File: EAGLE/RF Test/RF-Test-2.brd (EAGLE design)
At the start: 20.3 x 35.6 mm, 9 parts, among them X1 SMA-142-0701-881/886, X2 IPEX-20279-001E

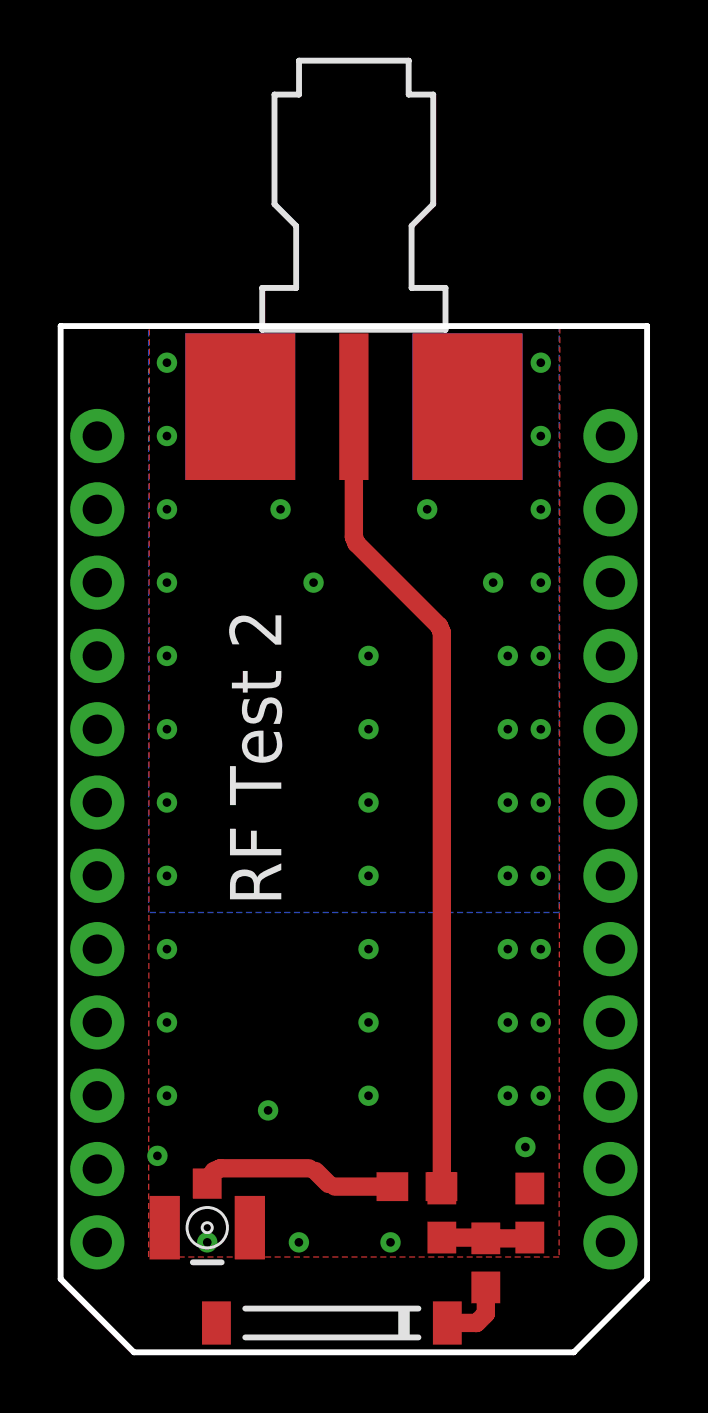
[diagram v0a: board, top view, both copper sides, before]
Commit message: RF Test board updated to match. A0 silk screen moved on core.
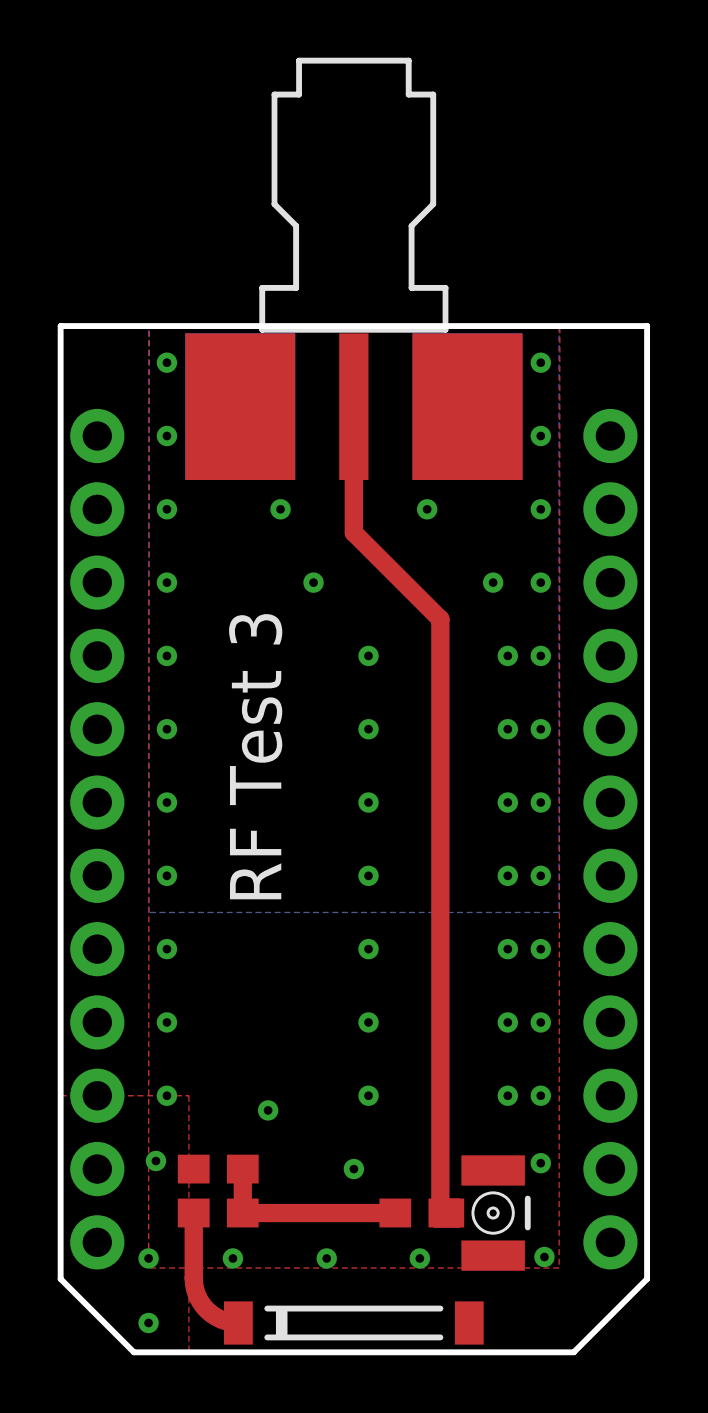
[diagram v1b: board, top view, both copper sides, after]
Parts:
- removed C12, C16: 10pF, rcl:C0603
- added C5: 10pF, rcl:C0603
- moved L1 10.9 mm to (5.46, 3.81), turned to 180 degrees
- moved X2 9.92 mm to (15.0, 2.29), turned to 90 degrees
- moved C4 9.43 mm to (5.46, 2.29), turned to 0 degrees
- moved ANT1 0.76 mm to (10.2, -1.52), turned to 180 degrees
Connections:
- removed net N$2: C16.2, X2.1
- net N$4: now also C5.2, X2.1; no longer C12.2, C16.1
- net N$5: now also C5.1; no longer C12.1
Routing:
- net N$2: track 6.96 -> 0.00 mm
- net N$5: track 3.07 -> 6.81 mm
- net N$3: track 2.38 -> 4.45 mm
- net N$4: track 28.4 -> 29.2 mm
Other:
- board text added: "RF Test 3"
- board text removed: "RF Test 2"
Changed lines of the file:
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@@
 <setting verticaltext="up"/>
 </settings>
-<grid distance="0.05" unitdist="inch" unit="inch" style="lines" multiple="1" display="yes" altdistance="0.005" altunitdist="inch" altunit="inch"/>
+<grid distance="2" unitdist="mil" unit="mil" style="lines" multiple="1" display="yes" altdistance="0.005" altunitdist="inch" altunit="inch"/>
 <layers>
 <layer number="1" name="Top" color="4" fill="1" visible="yes" active="yes"/>
-<layer number="2" name="$GND" color="13" fill="1" visible="no" active="yes"/>
+<layer number="2" name="$GND" color="13" fill="1" visible="yes" active="yes"/>
 <layer number="3" name="Route3" color="4" fill="3" visible="no" active="no"/>
 <layer number="4" name="Route4" color="1" fill="4" visible="no" active="no"/>
@@
 <wire x1="17.78" y1="0.508" x2="17.78" y2="29.21" width="0.2032" layer="51"/>
 <wire x1="2.54" y1="0.508" x2="2.54" y2="29.21" width="0.2032" layer="51"/>
-<text x="5.8674" y="23.2156" size="1.778" layer="21" rot="R270">RF Test 2</text>
+<text x="5.8674" y="23.2156" size="1.778" layer="21" rot="R270">RF Test 3</text>
 </plain>
 <attributes>
@@
 <class number="1" name="vcc" width="0" drill="0">
 </class>
-<class number="2" name="RF" width="0.5842" drill="0">
-<clearance class="2" value="0.762"/>
+<class number="2" name="RF" width="0.635" drill="0">
+<clearance class="2" value="0.635"/>
 </class>
 <class number="3" name="RF2" width="0.5842" drill="0">
@@
 <element name="JP1" library="SparkFun" package="1X12" value="" x="1.27" y="29.21" locked="yes" rot="MR270"/>
 <element name="JP2" library="SparkFun" package="1X12" value="" x="19.05" y="29.21" locked="yes" rot="MR270"/>
-<element name="L1" library="SparkFun-Passives" package="0603" value="2.2nH" x="16.256" y="2.286" smashed="yes" rot="R90">
-<attribute name="VALUE" x="16.51" y="-1.778" size="0.6096" layer="27" font="vector" rot="R90"/>
+<element name="L1" library="SparkFun-Passives" package="0603" value="2.2nH" x="5.461" y="3.81" smashed="yes" rot="R180">
+<attribute name="VALUE" x="9.525" y="4.064" size="0.6096" layer="27" font="vector" rot="R180"/>
 </element>
-<element name="C4" library="rcl" package="C0603" value="2.2pF" x="14.732" y="0.5588" smashed="yes" rot="R90">
-<attribute name="VALUE" x="15.494" y="0.3048" size="0.6096" layer="27"/>
+<element name="C4" library="rcl" package="C0603" value="2.2pF" x="5.461" y="2.286" smashed="yes">
+<attribute name="VALUE" x="5.207" y="1.524" size="0.6096" layer="27" rot="R270"/>
 </element>
-<element name="X2" library="Spark" package="IPEX-20279-001E" value="IPEX-20279-001E" x="5.08" y="1.778"/>
-<element name="C16" library="rcl" package="C0603" value="10pF" x="12.3444" y="3.2004" smashed="yes" rot="R180">
-<attribute name="VALUE" x="12.9794" y="5.1054" size="1.27" layer="27" rot="R180"/>
+<element name="X2" library="Spark" package="IPEX-20279-001E" value="IPEX-20279-001E" x="14.986" y="2.286" rot="R90"/>
+<element name="ANT1" library="Spark" package="AT8010" value="AT8010" x="10.16" y="-1.524" smashed="yes" rot="R180">
+<attribute name="VALUE" x="14.16" y="-0.424" size="0.4064" layer="27" rot="R180"/>
 </element>
-<element name="ANT1" library="Spark" package="AT8010" value="AT8010" x="9.398" y="-1.524" smashed="yes">
-<attribute name="VALUE" x="5.398" y="-2.624" size="0.4064" layer="27"/>
-</element>
-<element name="C12" library="rcl" package="C0603" value="10pF" x="13.208" y="2.286" smashed="yes" rot="R90">
-<attribute name="VALUE" x="15.113" y="1.651" size="1.27" layer="27" rot="R90"/>
+<element name="C5" library="rcl" package="C0603" value="10pF" x="12.446" y="2.286" smashed="yes">
+<attribute name="VALUE" x="11.811" y="0.381" size="1.27" layer="27"/>
 </element>
 <element name="X1" library="andyw-oct-2011" package="ANDYW-GENERIC-END-LAUNCH" value="SMA-142-0701-881/886" x="10.16" y="32.7914" smashed="yes" rot="R270">
@@
 <vertex x="0" y="33.02"/>
 <vertex x="20.32" y="33.02"/>
-<vertex x="20.32" y="0.762"/>
-<vertex x="0" y="0.762"/>
+<vertex x="20.32" y="0.381"/>
+<vertex x="0" y="0.381"/>
 </polygon>
-<via x="3.3528" y="4.2672" extent="1-16" drill="0.3"/>
+<via x="3.302" y="4.0894" extent="1-16" drill="0.3"/>
 <contactref element="X2" pad="2@1"/>
 <contactref element="X2" pad="2@2"/>
-<via x="5.08" y="1.27" extent="1-16" drill="0.3"/>
-<via x="8.255" y="1.27" extent="1-16" drill="0.3"/>
-<via x="11.43" y="1.27" extent="1-16" drill="0.3"/>
+<via x="3.048" y="-1.524" extent="1-16" drill="0.3"/>
+<via x="3.048" y="0.7112" extent="1-16" drill="0.3"/>
+<via x="10.16" y="3.81" extent="1-16" drill="0.3"/>
 <polygon width="0.1524" layer="1" thermals="no">
-<vertex x="3.048" y="0.762"/>
+<vertex x="3.048" y="0.381"/>
 <vertex x="3.0734" y="32.9692"/>
 <vertex x="17.2974" y="32.9692"/>
-<vertex x="17.272" y="0.762"/>
+<vertex x="17.272" y="0.381"/>
 </polygon>
 <contactref element="X1" pad="G@4"/>
@@
 <via x="3.683" y="6.35" extent="1-16" drill="0.3"/>
 <via x="7.1882" y="5.842" extent="1-16" drill="0.3"/>
-<via x="16.1036" y="4.572" extent="1-16" drill="0.3"/>
+<polygon width="0.1524" layer="2">
+<vertex x="4.445" y="6.35"/>
+<vertex x="4.445" y="-2.54"/>
+<vertex x="2.921" y="-2.54"/>
+<vertex x="2.54" y="-2.54"/>
+<vertex x="0.381" y="-0.381"/>
+<vertex x="0" y="0"/>
+<vertex x="0" y="5.715"/>
+<vertex x="0" y="6.35"/>
+</polygon>
+<polygon width="0.1524" layer="1">
+<vertex x="4.445" y="6.35"/>
+<vertex x="4.445" y="-2.54"/>
+<vertex x="2.921" y="-2.54"/>
+<vertex x="2.54" y="-2.54"/>
+<vertex x="0.381" y="-0.381"/>
+<vertex x="0" y="0"/>
+<vertex x="0" y="5.715"/>
+<vertex x="0" y="6.35"/>
+</polygon>
+<via x="5.969" y="0.7112" extent="1-16" drill="0.3"/>
+<via x="9.2202" y="0.7112" extent="1-16" drill="0.3"/>
+<via x="12.446" y="0.7112" extent="1-16" drill="0.3"/>
+<via x="16.764" y="0.762" extent="1-16" drill="0.3"/>
+<via x="16.637" y="4.0132" extent="1-16" drill="0.3"/>
 </signal>
 <signal name="RAW" class="1">
@@
 <contactref element="JP2" pad="9"/>
 </signal>
-<signal name="N$4" class="3">
-<contactref element="C16" pad="1"/>
-<contactref element="C12" pad="2"/>
-<wire x1="13.1944" y1="3.2004" x2="13.16" y2="3.2348" width="0.635" layer="1"/>
+<signal name="N$4" class="2">
+<contactref element="C5" pad="2"/>
 <contactref element="X1" pad="1"/>
-<wire x1="13.208" y1="3.136" x2="13.208" y2="22.3982875" width="0.635" layer="1"/>
-<wire x1="13.208" y1="22.3982875" x2="13.11500625" y2="22.62279375" width="0.635" layer="1"/>
-<wire x1="13.11500625" y1="22.62279375" x2="10.25299375" y2="25.48480625" width="0.635" layer="1"/>
-<wire x1="10.25299375" y1="25.48480625" x2="10.16" y2="25.7093125" width="0.635" layer="1"/>
-<wire x1="10.16" y1="25.7093125" x2="10.16" y2="30.226" width="0.635" layer="1"/>
-<wire x1="13.208" y1="3.136" x2="13.1944" y2="3.1496" width="0.4064" layer="1"/>
-<wire x1="13.1944" y1="3.1496" x2="13.1944" y2="3.2004" width="0.4064" layer="1"/>
+<contactref element="X2" pad="1"/>
+<wire x1="13.296" y1="2.286" x2="13.1572" y2="2.4248" width="0.635" layer="1" curve="-90"/>
+<wire x1="13.1572" y1="2.4248" x2="13.1572" y2="22.86" width="0.635" layer="1"/>
+<wire x1="13.1572" y1="22.86" x2="10.16" y2="25.8572" width="0.635" layer="1"/>
+<wire x1="10.16" y1="25.8572" x2="10.16" y2="30.226" width="0.635" layer="1"/>
+<wire x1="13.296" y1="2.286" x2="13.4585" y2="2.286" width="0" layer="19" extent="1-1"/>
 </signal>
 <signal name="!RST">
@@
 <signal name="VDDA">
 <contactref element="JP2" pad="3"/>
-</signal>
-<signal name="N$2" class="2">
-<contactref element="C16" pad="2"/>
-<contactref element="X2" pad="1"/>
-<wire x1="11.4944" y1="3.2004" x2="9.5041125" y2="3.2004" width="0.635" layer="1"/>
-<wire x1="9.5041125" y1="3.2004" x2="9.27960625" y2="3.29339375" width="0.5842" layer="1"/>
-<wire x1="9.27960625" y1="3.29339375" x2="8.83059375" y2="3.74240625" width="0.635" layer="1"/>
-<wire x1="8.83059375" y1="3.74240625" x2="8.6060875" y2="3.8354" width="0.5842" layer="1"/>
-<wire x1="8.6060875" y1="3.8354" x2="5.5290125" y2="3.8354" width="0.635" layer="1"/>
-<wire x1="5.5290125" y1="3.8354" x2="5.30450625" y2="3.74240625" width="0.635" layer="1"/>
-<wire x1="5.30450625" y1="3.74240625" x2="5.08" y2="3.5179" width="0.5842" layer="1"/>
-<wire x1="5.08" y1="3.5179" x2="5.08" y2="3.3055" width="0.5842" layer="1"/>
 </signal>
 <signal name="N$3" class="2">
 <contactref element="ANT1" pad="SIG"/>
 <contactref element="C4" pad="1"/>
-<wire x1="14.732" y1="-0.2912" x2="14.732" y2="-1.2065" width="0.635" layer="1"/>
-<wire x1="14.732" y1="-1.2065" x2="14.4145" y2="-1.524" width="0.635" layer="1"/>
-<wire x1="14.4145" y1="-1.524" x2="13.398" y2="-1.524" width="0.635" layer="1"/>
+<wire x1="6.16" y1="-1.524" x2="4.611" y2="0.025" width="0.635" layer="1" curve="-90"/>
+<wire x1="4.611" y1="0.025" x2="4.611" y2="2.286" width="0.635" layer="1"/>
 </signal>
 <signal name="N$5" class="2">
 <contactref element="C4" pad="2"/>
 <contactref element="L1" pad="1"/>
-<contactref element="C12" pad="1"/>
-<wire x1="13.208" y1="1.436" x2="14.7048" y2="1.436" width="0.635" layer="1"/>
-<wire x1="14.7048" y1="1.436" x2="14.732" y2="1.4088" width="0.635" layer="1"/>
-<wire x1="14.732" y1="1.4088" x2="16.2288" y2="1.4088" width="0.635" layer="1"/>
-<wire x1="16.2288" y1="1.4088" x2="16.256" y2="1.436" width="0.635" layer="1"/>
+<contactref element="C5" pad="1"/>
+<wire x1="11.596" y1="2.286" x2="6.311" y2="2.286" width="0.635" layer="1"/>
+<wire x1="6.311" y1="2.286" x2="6.311" y2="3.81" width="0.635" layer="1"/>
 </signal>
 </signals>
